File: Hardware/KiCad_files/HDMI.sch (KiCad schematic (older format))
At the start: 0 parts

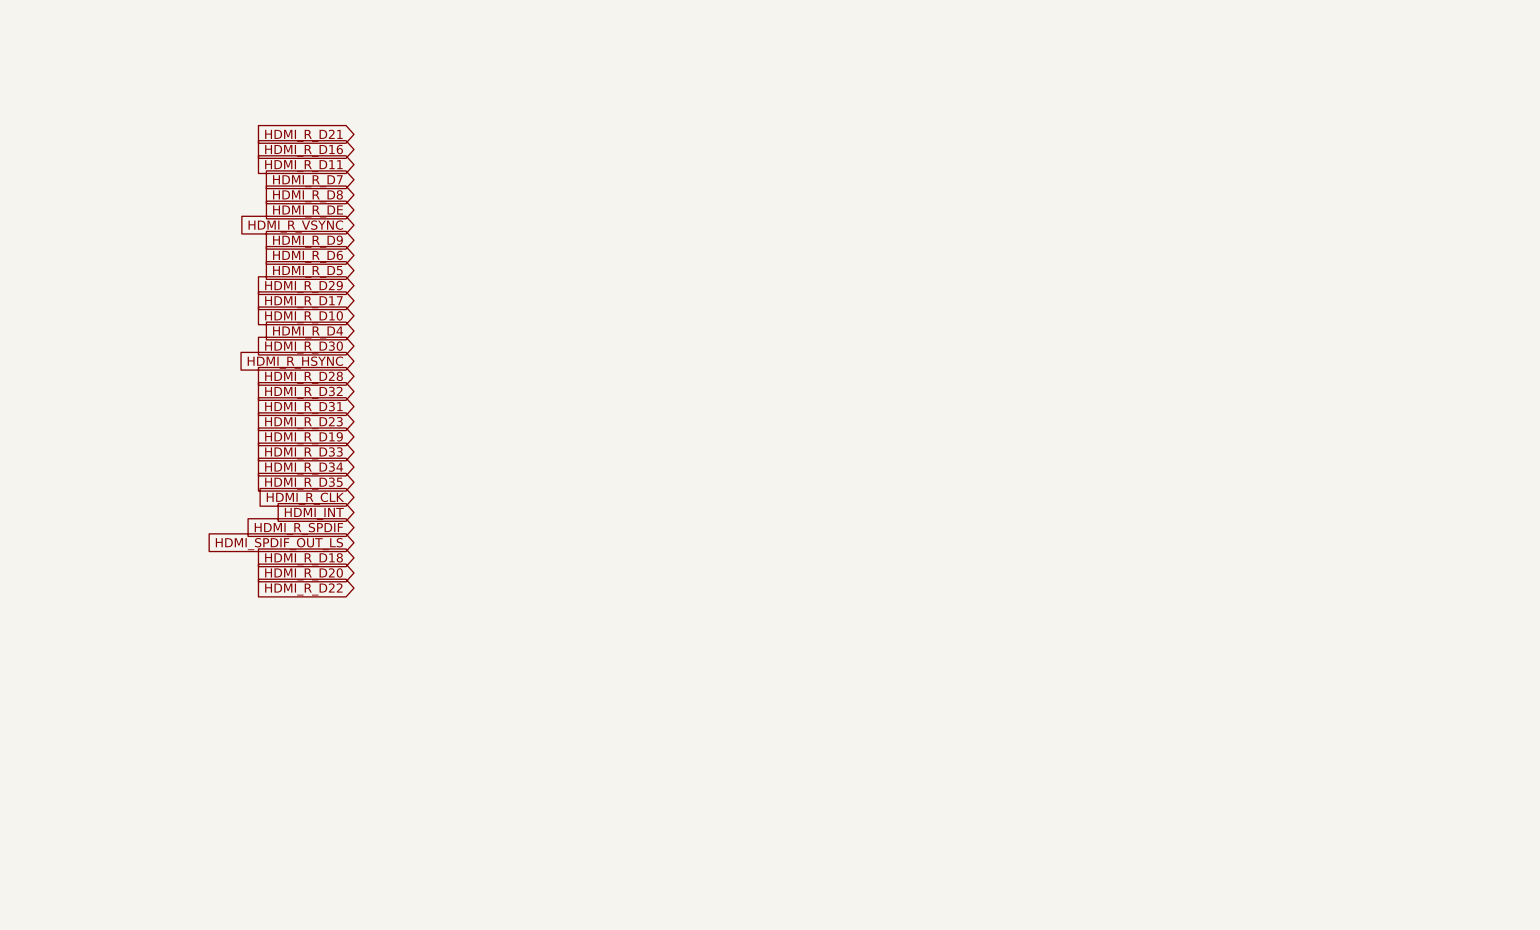
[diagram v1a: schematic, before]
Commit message: Added  HDMI transmitter chip
Also added resistors and moved HDMI data pins around on FPGA side
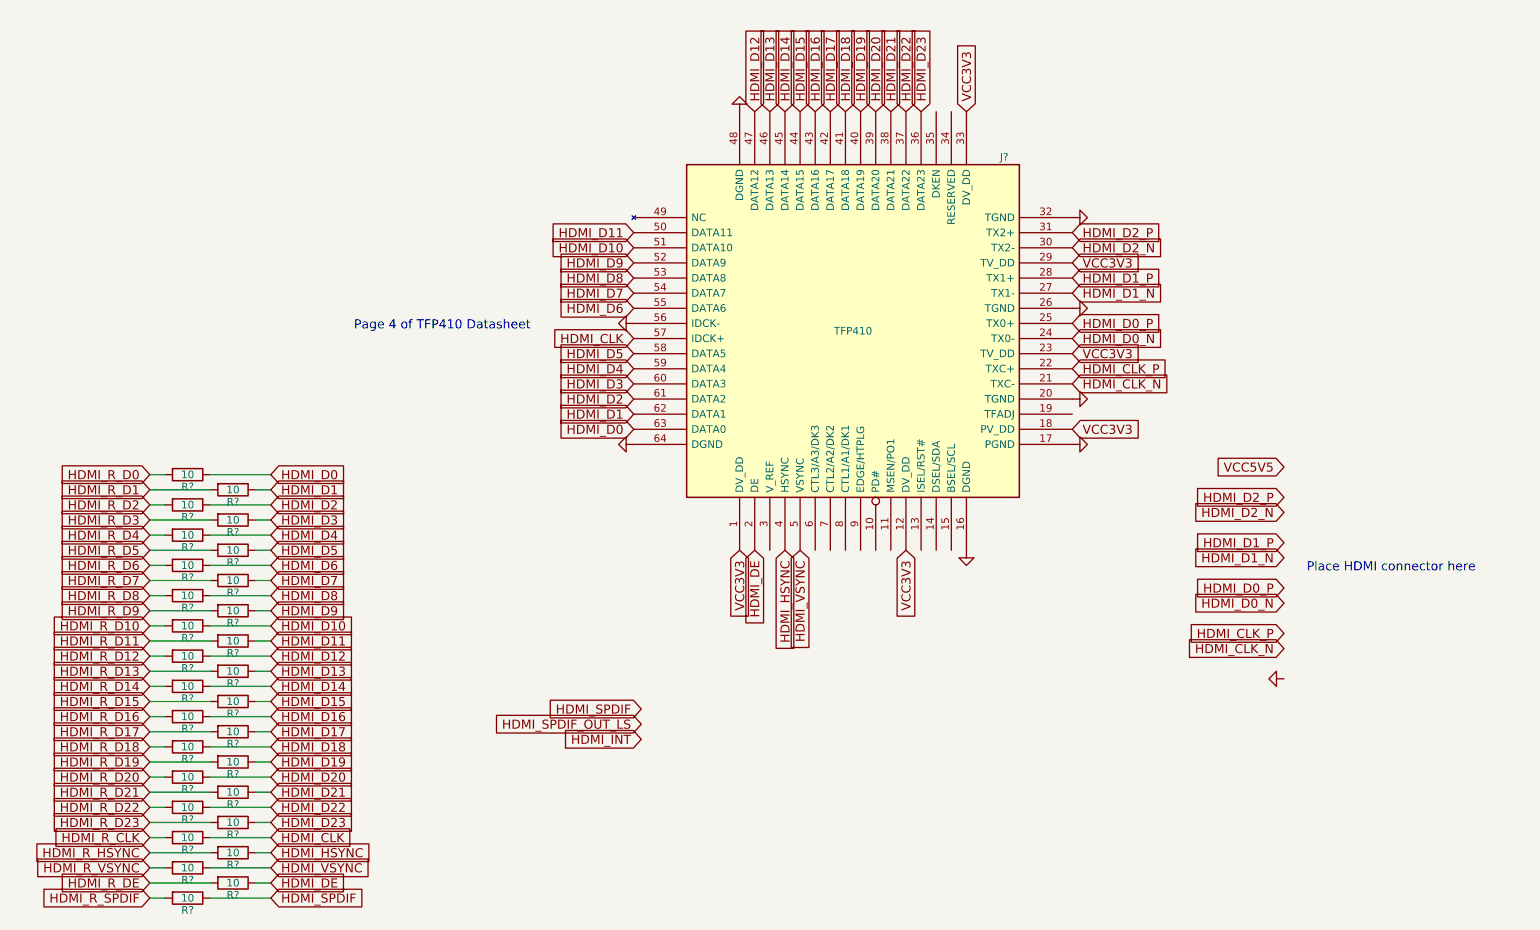
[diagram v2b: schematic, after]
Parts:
- added J?: TFP410, symbol TFP410
- added R? (x29): 10, symbol R
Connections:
- net HDMI_R_CLK: now also R?.2
- net HDMI_R_D10: now also R?.2
- net HDMI_R_D11: now also R?.2
- net HDMI_R_D16: now also R?.2
- net HDMI_R_D17: now also R?.2
- net HDMI_R_D18: now also R?.2
- net HDMI_R_D19: now also R?.2
- net HDMI_R_D20: now also R?.2
- net HDMI_R_D21: now also R?.2
- net HDMI_R_D22: now also R?.2
- net HDMI_R_D23: now also R?.2
- net HDMI_R_D4: now also R?.2
- net HDMI_R_D5: now also R?.2
- net HDMI_R_D6: now also R?.2
- net HDMI_R_D7: now also R?.2
- net HDMI_R_D8: now also R?.2
- net HDMI_R_D9: now also R?.2
- net HDMI_R_DE: now also R?.2
- net HDMI_R_HSYNC: now also R?.2
- net HDMI_R_SPDIF: now also R?.2
- net HDMI_R_VSYNC: now also R?.2
- new net GND: J?.16 (DGND), J?.17 (PGND), J?.20 (TGND), J?.26 (TGND), J?.32 (TGND), J?.48 (DGND), J?.56 (IDCK-), J?.64 (DGND)
- new net HDMI_CLK: J?.57 (IDCK+), R?.1
- new net HDMI_CLK_N: J?.21 (TXC-)
- new net HDMI_CLK_P: J?.22 (TXC+)
- new net HDMI_D0: J?.63 (DATA0), R?.1
- new net HDMI_D0_N: J?.24 (TX0-)
- new net HDMI_D0_P: J?.25 (TX0+)
- new net HDMI_D1: J?.62 (DATA1), R?.1
- new net HDMI_D10: J?.51 (DATA10), R?.1
- new net HDMI_D11: J?.50 (DATA11), R?.1
- new net HDMI_D12: J?.47 (DATA12), R?.1
- new net HDMI_D13: J?.46 (DATA13), R?.1
- new net HDMI_D14: J?.45 (DATA14), R?.1
- new net HDMI_D15: J?.44 (DATA15), R?.1
- new net HDMI_D16: J?.43 (DATA16), R?.1
- new net HDMI_D17: J?.42 (DATA17), R?.1
- new net HDMI_D18: J?.41 (DATA18), R?.1
- new net HDMI_D19: J?.40 (DATA19), R?.1
- new net HDMI_D1_N: J?.27 (TX1-)
- new net HDMI_D1_P: J?.28 (TX1+)
- new net HDMI_D2: J?.61 (DATA2), R?.1
- new net HDMI_D20: J?.39 (DATA20), R?.1
- new net HDMI_D21: J?.38 (DATA21), R?.1
- new net HDMI_D22: J?.37 (DATA22), R?.1
- new net HDMI_D23: J?.36 (DATA23), R?.1
- new net HDMI_D2_N: J?.30 (TX2-)
- new net HDMI_D2_P: J?.31 (TX2+)
- new net HDMI_D3: J?.60 (DATA3), R?.1
- new net HDMI_D4: J?.59 (DATA4), R?.1
- new net HDMI_D5: J?.58 (DATA5), R?.1
- new net HDMI_D6: J?.55 (DATA6), R?.1
- new net HDMI_D7: J?.54 (DATA7), R?.1
- new net HDMI_D8: J?.53 (DATA8), R?.1
- new net HDMI_D9: J?.52 (DATA9), R?.1
- new net HDMI_DE: J?.2 (DE), R?.1
- new net HDMI_HSYNC: J?.4 (HSYNC), R?.1
- new net HDMI_R_D0: R?.2
- new net HDMI_R_D1: R?.2
- new net HDMI_R_D12: R?.2
- new net HDMI_R_D13: R?.2
- new net HDMI_R_D14: R?.2
- new net HDMI_R_D15: R?.2
- new net HDMI_R_D2: R?.2
- new net HDMI_R_D3: R?.2
- new net HDMI_SPDIF: R?.1
- new net HDMI_VSYNC: J?.5 (VSYNC), R?.1
- new net VCC3V3: J?.1 (DV_DD), J?.12 (DV_DD), J?.18 (PV_DD), J?.23 (TV_DD), J?.29 (TV_DD), J?.33 (DV_DD)
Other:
- note added: "Page 4 of TFP410 Datasheet"
- note added: "Place HDMI connector here"
